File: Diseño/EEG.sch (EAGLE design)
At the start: 18 parts

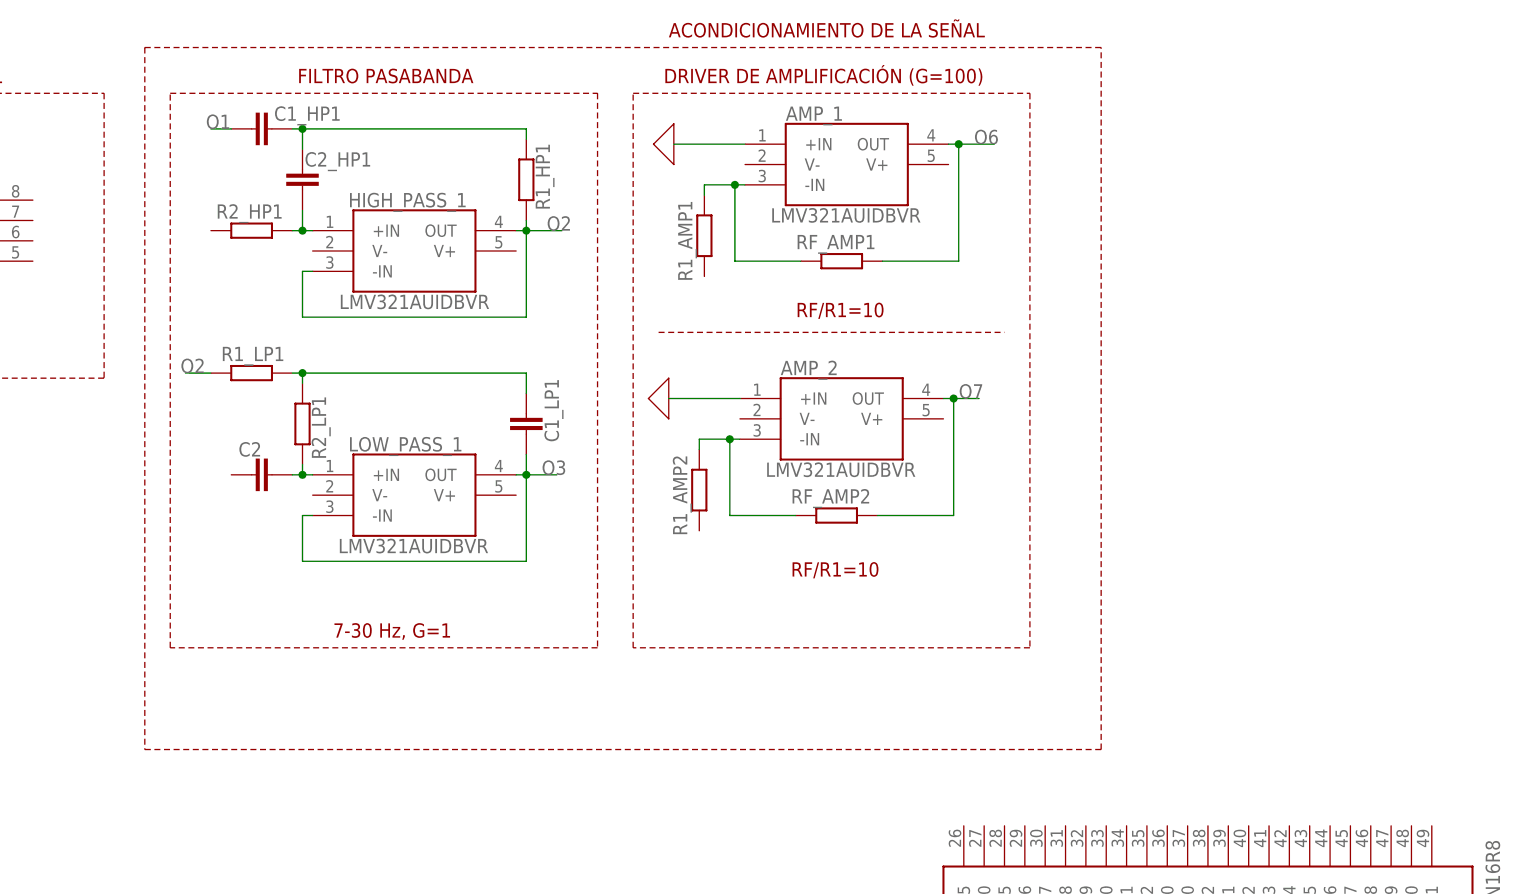
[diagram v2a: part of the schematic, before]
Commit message: Agregue el voltaje de referecia y conexiones de los amplificadores
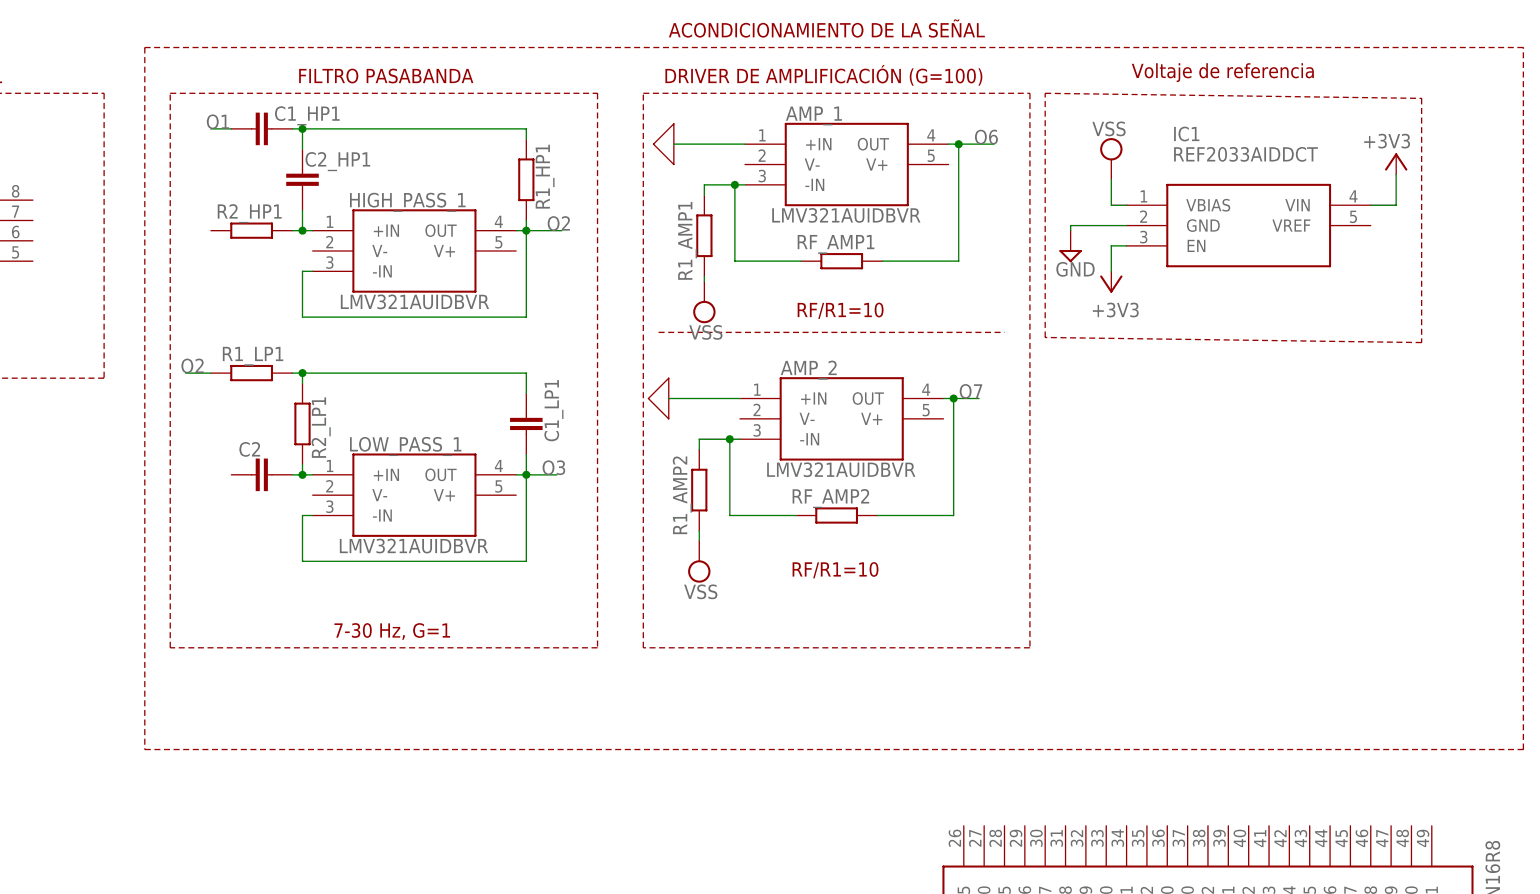
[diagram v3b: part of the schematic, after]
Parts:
- added IC1: REF2033AIDDCT, REF2033AIDDCT:REF2033AIDDCT
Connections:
- new net +3V3: IC1.EN, IC1.VIN
- new net GND: IC1.GND
- new net VSS: IC1.VBIAS, R1_AMP1.1, R1_AMP2.1
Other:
- note added: "Voltaje de referencia"
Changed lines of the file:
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@@
 <part name="INA_1" library="AD8226ARZ-R7" deviceset="AD8226ARZ-R7" device=""/>
 <part name="ESP32-S3" library="ESP32-S3-WROOM-1-N16R8" deviceset="ESP32-S3-WROOM-1-N16R8" device=""/>
+<part name="IC1" library="REF2033AIDDCT" deviceset="REF2033AIDDCT" device=""/>
+<part name="SUPPLY1" library="supply2" library_urn="urn:adsk.eagle:library:372" deviceset="VSS" device=""/>
+<part name="+3V1" library="supply1" library_urn="urn:adsk.eagle:library:371" deviceset="+3V3" device=""/>
+<part name="+3V2" library="supply1" library_urn="urn:adsk.eagle:library:371" deviceset="+3V3" device=""/>
+<part name="SUPPLY2" library="supply2" library_urn="urn:adsk.eagle:library:372" deviceset="GND" device=""/>
+<part name="SUPPLY3" library="supply2" library_urn="urn:adsk.eagle:library:372" deviceset="VSS" device=""/>
+<part name="SUPPLY4" library="supply2" library_urn="urn:adsk.eagle:library:372" deviceset="VSS" device=""/>
 </parts>
 <sheets>
@@
 <text x="29.845" y="170.18" size="1.778" layer="94">CAPTURA DE LA SEÑAL</text>
 <wire x1="73.025" y1="174.625" x2="73.025" y2="86.995" width="0.1524" layer="94" style="shortdash"/>
-<wire x1="73.025" y1="86.995" x2="192.405" y2="86.995" width="0.1524" layer="94" style="shortdash"/>
-<wire x1="192.405" y1="86.995" x2="192.405" y2="174.625" width="0.1524" layer="94" style="shortdash"/>
-<wire x1="192.405" y1="174.625" x2="73.025" y2="174.625" width="0.1524" layer="94" style="shortdash"/>
+<wire x1="73.025" y1="86.995" x2="245.11" y2="86.995" width="0.1524" layer="94" style="shortdash"/>
+<wire x1="245.11" y1="86.995" x2="245.11" y2="174.625" width="0.1524" layer="94" style="shortdash"/>
+<wire x1="245.11" y1="174.625" x2="73.025" y2="174.625" width="0.1524" layer="94" style="shortdash"/>
 <text x="138.43" y="175.895" size="1.778" layer="94">ACONDICIONAMIENTO DE LA SEÑAL</text>
 <text x="92.075" y="170.18" size="1.778" layer="94">FILTRO PASABANDA</text>
@@
 <wire x1="129.54" y1="99.695" x2="76.2" y2="99.695" width="0.1524" layer="94" style="shortdash"/>
 <wire x1="76.2" y1="99.695" x2="76.2" y2="168.91" width="0.1524" layer="94" style="shortdash"/>
-<wire x1="133.985" y1="168.91" x2="183.515" y2="168.91" width="0.1524" layer="94" style="shortdash"/>
+<wire x1="135.255" y1="168.91" x2="183.515" y2="168.91" width="0.1524" layer="94" style="shortdash"/>
 <wire x1="183.515" y1="168.91" x2="183.515" y2="99.695" width="0.1524" layer="94" style="shortdash"/>
-<wire x1="183.515" y1="99.695" x2="133.985" y2="99.695" width="0.1524" layer="94" style="shortdash"/>
-<wire x1="133.985" y1="99.695" x2="133.985" y2="168.91" width="0.1524" layer="94" style="shortdash"/>
+<wire x1="183.515" y1="99.695" x2="135.255" y2="99.695" width="0.1524" layer="94" style="shortdash"/>
+<wire x1="135.255" y1="99.695" x2="135.255" y2="168.91" width="0.1524" layer="94" style="shortdash"/>
 <text x="96.52" y="100.965" size="1.778" layer="94">7-30 Hz, G=1</text>
 <text x="154.305" y="140.97" size="1.778" layer="94">RF/R1=10</text>
 <text x="153.67" y="108.585" size="1.778" layer="94">RF/R1=10</text>
 <wire x1="137.16" y1="139.065" x2="180.34" y2="139.065" width="0.1524" layer="94" style="dashdot"/>
+<wire x1="185.42" y1="168.91" x2="232.41" y2="168.275" width="0.1524" layer="94" style="shortdash"/>
+<wire x1="232.41" y1="168.275" x2="232.41" y2="137.795" width="0.1524" layer="94" style="shortdash"/>
+<wire x1="232.41" y1="137.795" x2="185.42" y2="138.43" width="0.1524" layer="94" style="shortdash"/>
+<wire x1="185.42" y1="138.43" x2="185.42" y2="168.91" width="0.1524" layer="94" style="shortdash"/>
+<text x="196.215" y="170.815" size="1.778" layer="94">Voltaje de referencia</text>
 </plain>
 <instances>
@@
 <attribute name="NAME" x="171.45" y="50.8" size="1.778" layer="95" rot="R90" align="center-left"/>
 <attribute name="VALUE" x="241.3" y="45.085" size="1.778" layer="96" rot="R90" align="center-left"/>
+</instance>
+<instance part="IC1" gate="G$1" x="195.58" y="154.94" smashed="yes">
+<attribute name="NAME" x="201.295" y="163.83" size="1.778" layer="95" align="center-left"/>
+<attribute name="VALUE" x="201.295" y="161.29" size="1.778" layer="96" align="center-left"/>
+</instance>
+<instance part="SUPPLY1" gate="G$1" x="193.675" y="160.655" smashed="yes" rot="R180">
+<attribute name="VALUE" x="195.58" y="165.354" size="1.778" layer="96" rot="R180"/>
+</instance>
+<instance part="+3V1" gate="G$1" x="229.235" y="161.29" smashed="yes">
+<attribute name="VALUE" x="231.14" y="163.83" size="1.778" layer="96" rot="R180"/>
+</instance>
+<instance part="+3V2" gate="G$1" x="193.675" y="144.145" smashed="yes" rot="R180">
+<attribute name="VALUE" x="191.135" y="140.97" size="1.778" layer="96"/>
+</instance>
+<instance part="SUPPLY2" gate="GND" x="188.595" y="149.225" smashed="yes">
+<attribute name="VALUE" x="186.69" y="146.05" size="1.778" layer="96"/>
+</instance>
+<instance part="SUPPLY3" gate="G$1" x="142.875" y="142.875" smashed="yes">
+<attribute name="VALUE" x="140.97" y="138.176" size="1.778" layer="96"/>
+</instance>
+<instance part="SUPPLY4" gate="G$1" x="142.24" y="110.49" smashed="yes">
+<attribute name="VALUE" x="140.335" y="105.791" size="1.778" layer="96"/>
 </instance>
 </instances>
@@
 </segment>
 </net>
+<net name="VSS" class="0">
+<segment>
+<pinref part="SUPPLY1" gate="G$1" pin="VSS"/>
+<pinref part="IC1" gate="G$1" pin="VBIAS"/>
+<wire x1="193.675" y1="158.115" x2="193.675" y2="154.94" width="0.1524" layer="91"/>
+<wire x1="193.675" y1="154.94" x2="195.58" y2="154.94" width="0.1524" layer="91"/>
+</segment>
+<segment>
+<pinref part="R1_AMP1" gate="G$1" pin="1"/>
+<pinref part="SUPPLY3" gate="G$1" pin="VSS"/>
+<wire x1="142.875" y1="146.05" x2="142.875" y2="145.415" width="0.1524" layer="91"/>
+</segment>
+<segment>
+<pinref part="R1_AMP2" gate="G$1" pin="1"/>
+<pinref part="SUPPLY4" gate="G$1" pin="VSS"/>
+<wire x1="142.24" y1="114.3" x2="142.24" y2="113.03" width="0.1524" layer="91"/>
+</segment>
+</net>
+<net name="+3V3" class="0">
+<segment>
+<pinref part="+3V1" gate="G$1" pin="+3V3"/>
+<pinref part="IC1" gate="G$1" pin="VIN"/>
+<wire x1="229.235" y1="158.75" x2="229.235" y2="154.94" width="0.1524" layer="91"/>
+<wire x1="229.235" y1="154.94" x2="226.06" y2="154.94" width="0.1524" layer="91"/>
+</segment>
+<segment>
+<pinref part="+3V2" gate="G$1" pin="+3V3"/>
+<wire x1="193.675" y1="146.685" x2="193.675" y2="149.86" width="0.1524" layer="91"/>
+<wire x1="193.675" y1="149.86" x2="195.58" y2="149.86" width="0.1524" layer="91"/>
+<pinref part="IC1" gate="G$1" pin="EN"/>
+</segment>
+</net>
+<net name="GND" class="0">
+<segment>
+<pinref part="SUPPLY2" gate="GND" pin="GND"/>
+<wire x1="188.595" y1="151.765" x2="188.595" y2="152.4" width="0.1524" layer="91"/>
+<pinref part="IC1" gate="G$1" pin="GND"/>
+<wire x1="188.595" y1="152.4" x2="195.58" y2="152.4" width="0.1524" layer="91"/>
+</segment>
+</net>
